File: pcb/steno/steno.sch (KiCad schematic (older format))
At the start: 60 parts, among them J1 USB_mini_micro_B, K1 PG1350, K10 PG1350, K11 PG1350, K12 PG1350, K13 PG1350, K14 PG1350, K15 PG1350, K16 PG1350, K17 PG1350, K18 PG1350, K19 PG1350, K2 PG1350, K20 PG1350, K21 PG1350, K22 PG1350, K23 PG1350, K24 PG1350, K25 PG1350, K26 PG1350, K27 PG1350, K28 PG1350, K29 PG1350, K3 PG1350, K30 PG1350, K4 PG1350, K5 PG1350, K6 PG1350, K7 PG1350, K8 PG1350, K9 PG1350, SW1 SW_Push, SW2 SW_Push, U1 ATmega32U4-AU, U2 MT25QL128ABA1ESE, U3 MCP1700-3302E_SOT23, U4 LCD2.2in, U5 4050, Y1 16MHz

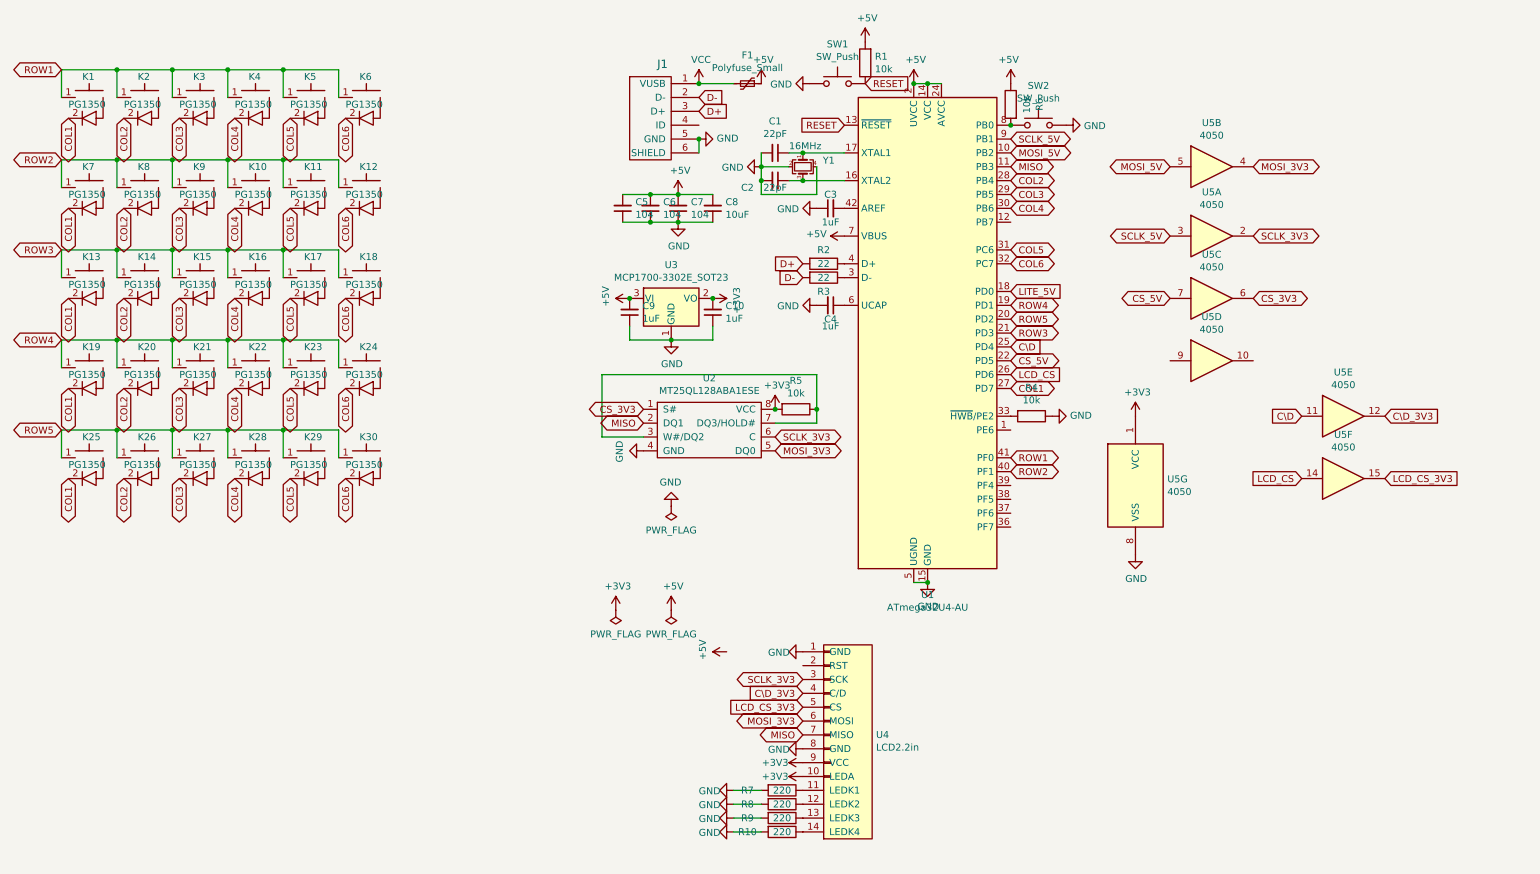
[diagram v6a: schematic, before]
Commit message: [PCB] Change to USB-C connector + protection diode
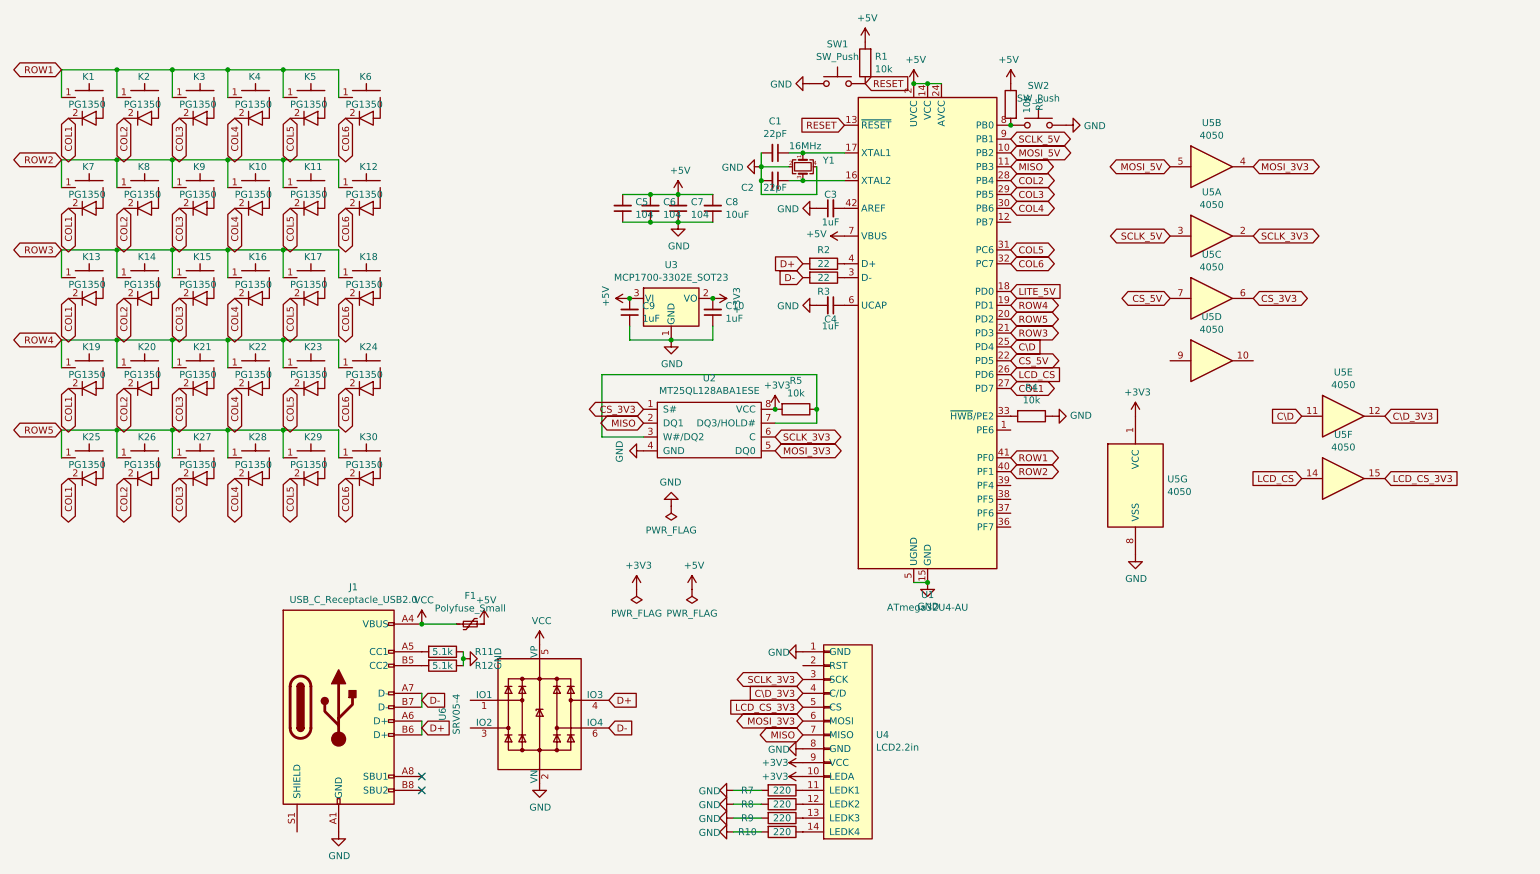
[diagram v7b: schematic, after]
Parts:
- removed J1: USB_mini_micro_B, Connector_USB:AMPHENOL_10118192-0001LF, symbol keyboard_parts:USB_mini_micro_B
- added J1: USB_C_Receptacle_USB2.0, Connector_USB:USB_C_Receptacle_HRO_TYPE-C-31-M-12, symbol Connector:USB_C_Receptacle_USB2.0
- added R11, R12: 5.1k, Resistor_SMD:R_0603_1608Metric, symbol Device:R
- added U6: SRV05-4, Package_TO_SOT_SMD:SOT-23-6, symbol Power_Protection:SRV05-4
- Y1: footprint Crystal:Crystal_SMD_EuroQuartz_MJ-4Pin_5.0x3.2mm -> Crystal:Crystal_SMD_EuroQuartz_MT-4Pin_3.2x2.5mm
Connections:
- net D+: now also J1.A6 (D+), J1.B6 (D+), U6.4 (IO3)
- net D-: now also J1.A7 (D-), J1.B7 (D-), U6.6 (IO4)
- net GND: now also J1.A1 (GND), J1.A12 (GND), J1.B1 (GND), J1.B12 (GND), R11.1, R12.1, U6.2 (VN)
- net VCC: now also J1.A4 (VBUS), J1.A9 (VBUS), J1.B4 (VBUS), J1.B9 (VBUS), U6.5 (VP)
- new net: J1.A5 (CC1), R11.2
- new net: J1.B5 (CC2), R12.2
- no-connect marks 0 -> 2
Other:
- moved on the sheet: F1
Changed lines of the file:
@@
-$EndComp
-$Comp
-L keyboard_parts:USB_mini_micro_B J1
-U 1 1 5F6E22DC
-P 5450 950
-F 0 "J1" H 5337 1241 60  0000 C CNN
-F 1 "USB_mini_micro_B" H 5300 1200 60  0001 C CNN
-F 2 "Connector_USB:AMPHENOL_10118192-0001LF" H 5400 950 60  0001 C CNN
-F 3 "" H 5400 950 60  0000 C CNN
-	1    5450 950
-	1    0    0    -1
 $EndComp
 $Comp
@@
 F 0 "Y1" V 6304 1544 50  0000 L CNN
 F 1 "16MHz" V 6200 1300 50  0000 L CNN
-F 2 "Crystal:Crystal_SMD_EuroQuartz_MJ-4Pin_5.0x3.2mm" H 6350 1400 50  0001 C CNN
+F 2 "Crystal:Crystal_SMD_EuroQuartz_MT-4Pin_3.2x2.5mm" H 6350 1400 50  0001 C CNN
 F 3 "~" H 6350 1400 50  0001 C CNN
 	1    6350 1400
@@
 L Device:Polyfuse_Small F1
 U 1 1 5F6EA8C1
-P 5950 800
-F 0 "F1" V 5745 800 50  0000 C CNN
-F 1 "Polyfuse_Small" V 5836 800 50  0000 C CNN
-F 2 "Fuse:Fuse_1206_3216Metric_Castellated" H 6000 600 50  0001 L CNN
-F 3 "~" H 5950 800 50  0001 C CNN
-	1    5950 800
+P 3950 4700
+F 0 "F1" V 3745 4700 50  0000 C CNN
+F 1 "Polyfuse_Small" V 3836 4700 50  0000 C CNN
+F 2 "Fuse:Fuse_1206_3216Metric_Castellated" H 4000 4500 50  0001 L CNN
+F 3 "~" H 3950 4700 50  0001 C CNN
+	1    3950 4700
 	0    1    1    0
 $EndComp
@@
 L power:PWR_FLAG #FLG01
 U 1 1 5F79174E
-P 5000 4600
-F 0 "#FLG01" H 5000 4675 50  0001 C CNN
-F 1 "PWR_FLAG" H 5000 4773 50  0000 C CNN
-F 2 "" H 5000 4600 50  0001 C CNN
-F 3 "~" H 5000 4600 50  0001 C CNN
-	1    5000 4600
+P 5150 4450
+F 0 "#FLG01" H 5150 4525 50  0001 C CNN
+F 1 "PWR_FLAG" H 5150 4623 50  0000 C CNN
+F 2 "" H 5150 4450 50  0001 C CNN
+F 3 "~" H 5150 4450 50  0001 C CNN
+	1    5150 4450
 	-1   0    0    1
 $EndComp
@@
 L power:+3V3 #PWR021
 U 1 1 5F791D12
-P 5000 4600
-F 0 "#PWR021" H 5000 4450 50  0001 C CNN
-F 1 "+3V3" H 5015 4773 50  0000 C CNN
-F 2 "" H 5000 4600 50  0001 C CNN
-F 3 "" H 5000 4600 50  0001 C CNN
-	1    5000 4600
+P 5150 4450
+F 0 "#PWR021" H 5150 4300 50  0001 C CNN
+F 1 "+3V3" H 5165 4623 50  0000 C CNN
+F 2 "" H 5150 4450 50  0001 C CNN
+F 3 "" H 5150 4450 50  0001 C CNN
+	1    5150 4450
 	1    0    0    -1
 $EndComp
@@
 $EndComp
 $Comp
-L power:GND #PWR05
-U 1 1 5F79E9E5
-P 5600 1200
-F 0 "#PWR05" H 5600 950 50  0001 C CNN
-F 1 "GND" V 5605 1072 50  0000 R CNN
-F 2 "" H 5600 1200 50  0001 C CNN
-F 3 "" H 5600 1200 50  0001 C CNN
-	1    5600 1200
-	0    -1   -1   0
-$EndComp
-Wire Wire Line
-	5600 1200 5600 1300
-Connection ~ 5600 1200
-Text GLabel 5600 900  2    50   Input ~ 0
-D-
-Text GLabel 5600 1000 2    50   Input ~ 0
-D+
-$Comp
 L power:VCC #PWR01
 U 1 1 5F7A2679
-P 5600 800
-F 0 "#PWR01" H 5600 650 50  0001 C CNN
-F 1 "VCC" H 5615 973 50  0000 C CNN
-F 2 "" H 5600 800 50  0001 C CNN
-F 3 "" H 5600 800 50  0001 C CNN
-	1    5600 800
-	1    0    0    -1
-$EndComp
-Wire Wire Line
-	5850 800  5600 800
-Connection ~ 5600 800
+P 3600 4700
+F 0 "#PWR01" H 3600 4550 50  0001 C CNN
+F 1 "VCC" H 3615 4873 50  0000 C CNN
+F 2 "" H 3600 4700 50  0001 C CNN
+F 3 "" H 3600 4700 50  0001 C CNN
+	1    3600 4700
+	1    0    0    -1
+$EndComp
+Wire Wire Line
+	3850 4700 3600 4700
 $Comp
 L power:+5V #PWR02
 U 1 1 5F7AC381
-P 6050 800
-F 0 "#PWR02" H 6050 650 50  0001 C CNN
-F 1 "+5V" H 6065 973 50  0000 C CNN
-F 2 "" H 6050 800 50  0001 C CNN
-F 3 "" H 6050 800 50  0001 C CNN
-	1    6050 800
+P 4050 4700
+F 0 "#PWR02" H 4050 4550 50  0001 C CNN
+F 1 "+5V" H 4065 4873 50  0000 C CNN
+F 2 "" H 4050 4700 50  0001 C CNN
+F 3 "" H 4050 4700 50  0001 C CNN
+	1    4050 4700
 	1    0    0    -1
 $EndComp
@@
 L power:+5V #PWR022
 U 1 1 5F7935BA
-P 5400 4600
-F 0 "#PWR022" H 5400 4450 50  0001 C CNN
-F 1 "+5V" H 5415 4773 50  0000 C CNN
-F 2 "" H 5400 4600 50  0001 C CNN
-F 3 "" H 5400 4600 50  0001 C CNN
-	1    5400 4600
+P 5550 4450
+F 0 "#PWR022" H 5550 4300 50  0001 C CNN
+F 1 "+5V" H 5565 4623 50  0000 C CNN
+F 2 "" H 5550 4450 50  0001 C CNN
+F 3 "" H 5550 4450 50  0001 C CNN
+	1    5550 4450
 	1    0    0    -1
 $EndComp
@@
 L power:PWR_FLAG #FLG02
 U 1 1 5F790BAA
-P 5400 4600
-F 0 "#FLG02" H 5400 4675 50  0001 C CNN
-F 1 "PWR_FLAG" H 5400 4773 50  0000 C CNN
-F 2 "" H 5400 4600 50  0001 C CNN
-F 3 "~" H 5400 4600 50  0001 C CNN
-	1    5400 4600
+P 5550 4450
+F 0 "#FLG02" H 5550 4525 50  0001 C CNN
+F 1 "PWR_FLAG" H 5550 4623 50  0000 C CNN
+F 2 "" H 5550 4450 50  0001 C CNN
+F 3 "~" H 5550 4450 50  0001 C CNN
+	1    5550 4450
 	-1   0    0    1
 $EndComp
@@
 Text GLabel 7850 2800 2    50   BiDi ~ 0
 CS_5V
-$Comp
-L power:+5V #PWR0101
-U 1 1 5F7617F8
-P 5800 4900
-F 0 "#PWR0101" H 5800 4750 50  0001 C CNN
-F 1 "+5V" H 5815 5073 50  0000 C CNN
-F 2 "" H 5800 4900 50  0001 C CNN
-F 3 "" H 5800 4900 50  0001 C CNN
-	1    5800 4900
-	0    -1   -1   0
-$EndComp
 Text GLabel 9000 2350 0    50   BiDi ~ 0
 CS_5V
@@
 Wire Wire Line
 	3000 3500 3000 3300
+$Comp
+L Connector:USB_C_Receptacle_USB2.0 J1
+U 1 1 603A274B
+P 3000 5300
+F 0 "J1" H 3107 6167 50  0000 C CNN
+F 1 "USB_C_Receptacle_USB2.0" H 3107 6076 50  0000 C CNN
+F 2 "Connector_USB:USB_C_Receptacle_HRO_TYPE-C-31-M-12" H 3150 5300 50  0001 C CNN
+F 3 "https://www.usb.org/sites/default/files/documents/usb_type-c.zip" H 3150 5300 50  0001 C CNN
+	1    3000 5300
+	1    0    0    -1
+$EndComp
+$Comp
+L Device:R R11
+U 1 1 60403035
+P 3750 4900
+F 0 "R11" V 3750 5200 50  0000 C CNN
+F 1 "5.1k" V 3750 4900 50  0000 C CNN
+F 2 "Resistor_SMD:R_0603_1608Metric" V 3680 4900 50  0001 C CNN
+F 3 "~" H 3750 4900 50  0001 C CNN
+	1    3750 4900
+	0    1    1    0
+$EndComp
+$Comp
+L Device:R R12
+U 1 1 604188A6
+P 3750 5000
+F 0 "R12" V 3750 5300 50  0000 C CNN
+F 1 "5.1k" V 3750 5000 50  0000 C CNN
+F 2 "Resistor_SMD:R_0603_1608Metric" V 3680 5000 50  0001 C CNN
+F 3 "~" H 3750 5000 50  0001 C CNN
+	1    3750 5000
+	0    1    1    0
+$EndComp
+$Comp
+L power:GND #PWR0101
+U 1 1 6041F327
+P 3900 4950
+F 0 "#PWR0101" H 3900 4700 50  0001 C CNN
+F 1 "GND" H 3900 4700 50  0000 C CNN
+F 2 "" H 3900 4950 50  0001 C CNN
+F 3 "" H 3900 4950 50  0001 C CNN
+	1    3900 4950
+	0    -1   -1   0
+$EndComp
+$Comp
+L power:GND #PWR0116
+U 1 1 6042B16E
+P 4450 5850
+F 0 "#PWR0116" H 4450 5600 50  0001 C CNN
+F 1 "GND" H 4455 5677 50  0000 C CNN
+F 2 "" H 4450 5850 50  0001 C CNN
+F 3 "" H 4450 5850 50  0001 C CNN
+	1    4450 5850
+	1    0    0    -1
+$EndComp
+NoConn ~ 3600 5800
+NoConn ~ 3600 5900
+$Comp
+L power:GND #PWR0117
+U 1 1 60437D30
+P 3000 6200
+F 0 "#PWR0117" H 3000 5950 50  0001 C CNN
+F 1 "GND" H 3005 6027 50  0000 C CNN
+F 2 "" H 3000 6200 50  0001 C CNN
+F 3 "" H 3000 6200 50  0001 C CNN
+	1    3000 6200
+	1    0    0    -1
+$EndComp
+Wire Wire Line
+	3900 4900 3900 4950
+Connection ~ 3900 4950
+Wire Wire Line
+	3900 4950 3900 5000
+Connection ~ 3600 4700
+$Comp
+L Power_Protection:SRV05-4 U6
+U 1 1 603A89FD
+P 4450 5350
+F 0 "U6" V 3750 5350 50  0000 C CNN
+F 1 "SRV05-4" V 3850 5350 50  0000 C CNN
+F 2 "Package_TO_SOT_SMD:SOT-23-6" H 5150 4900 50  0001 C CNN
+F 3 "http://www.onsemi.com/pub/Collateral/SRV05-4-D.PDF" H 4450 5350 50  0001 C CNN
+	1    4450 5350
+	1    0    0    -1
+$EndComp
+$Comp
+L power:VCC #PWR0115
+U 1 1 60532A81
+P 4450 4850
+F 0 "#PWR0115" H 4450 4700 50  0001 C CNN
+F 1 "VCC" H 4465 5023 50  0000 C CNN
+F 2 "" H 4450 4850 50  0001 C CNN
+F 3 "" H 4450 4850 50  0001 C CNN
+	1    4450 4850
+	1    0    0    -1
+$EndComp
+Text GLabel 3600 5450 2    50   Input ~ 0
+D+
+Text GLabel 3600 5250 2    50   Input ~ 0
+D-
+Text GLabel 4950 5250 2    50   Input ~ 0
+D+
+Text GLabel 4950 5450 2    50   Input ~ 0
+D-
+Wire Wire Line
+	3600 5400 3600 5500
+Wire Wire Line
+	3600 5200 3600 5300
 $EndSCHEMATC

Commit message: [PCB] Public test version
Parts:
- removed R1, R6: 10k, Resistor_SMD:R_0805_2012Metric, symbol Device:R
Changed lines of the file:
@@
 Connection ~ 7250 4400
-$Comp
-L Device:R R1
-U 1 1 5F7CE710
-P 6800 650
-F 0 "R1" H 6730 604 50  0000 R CNN
-F 1 "10k" H 6730 695 50  0000 R CNN
-F 2 "Resistor_SMD:R_0805_2012Metric" V 6730 650 50  0001 C CNN
-F 3 "~" H 6800 650 50  0001 C CNN
-	1    6800 650
-	-1   0    0    1
-$EndComp
-$Comp
-L power:+5V #PWR03
-U 1 1 5F7CF7B2
-P 6800 500
-F 0 "#PWR03" H 6800 350 50  0001 C CNN
-F 1 "+5V" H 6815 673 50  0000 C CNN
-F 2 "" H 6800 500 50  0001 C CNN
-F 3 "" H 6800 500 50  0001 C CNN
-	1    6800 500
-	1    0    0    -1
-$EndComp
 $Comp
 L power:GND #PWR06
@@
 $EndComp
 $Comp
-L Device:R R6
-U 1 1 602A898A
-P 7850 950
-F 0 "R6" V 7643 950 50  0000 C CNN
-F 1 "10k" V 7734 950 50  0000 C CNN
-F 2 "Resistor_SMD:R_0805_2012Metric" V 7780 950 50  0001 C CNN
-F 3 "~" H 7850 950 50  0001 C CNN
-	1    7850 950
-	-1   0    0    -1
-$EndComp
-$Comp
 L Switch:SW_Push SW2
 U 1 1 602B341B
@@
 $EndComp
 $Comp
-L power:+5V #PWR0104
-U 1 1 602B3E68
-P 7850 800
-F 0 "#PWR0104" H 7850 650 50  0001 C CNN
-F 1 "+5V" H 7865 973 50  0000 C CNN
-F 2 "" H 7850 800 50  0001 C CNN
-F 3 "" H 7850 800 50  0001 C CNN
-	1    7850 800
-	-1   0    0    -1
-$EndComp
-$Comp
 L power:GND #PWR0105
 U 1 1 602B4471
@@
 	0    -1   1    0
 $EndComp
-Connection ~ 7850 1100
 $Comp
 L power:GND #PWR0106
